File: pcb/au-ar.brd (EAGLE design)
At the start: 65 x 45 mm, 74 parts, among them U1 TPD12S520DBTR, U2 TPD12S521DBTR

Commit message: added final edits for v1 order and pcbway gerbers
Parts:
- added FLASH: 0532610571, volks73-Molex:PICOBLADE53261-0571
- moved R30 2.30 mm to (7.49, 23.9)
- moved R29 2.27 mm to (7.42, 21.6)
- moved C8 1.21 mm to (16.7, 6.55), turned to 270 degrees
- moved CAMERA1 0.60 mm to (58.2, 29.7)
- moved CAMERA2 0.37 mm to (58.2, 15.2)
- moved C3 0.25 mm to (23.9, 24.5)
- moved C7 0.08 mm to (27.3, 6.93)
- moved C10 0.05 mm to (3.86, 23.9), turned to 180 degrees
- renumbered LINE_2_1 to 1, LINE_2_2 to 2, LINE_2_3 to 3, LINE_2_4 to 4
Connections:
- net 5V: no longer B1.BB_1, B1.BB_50, B1.DB_1, B1.DB_50
- net GND: now also FLASH.1
- net SPI_CLK: now also FLASH.2
- net SPI_CS: now also FLASH.5
- net SPI_DI: now also FLASH.3
- net SPI_DO: now also FLASH.4
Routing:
- net 3V3: track 25.1 -> 97.9 mm, vias 11 -> 33
- net GND: track 108.4 -> 176.6 mm, vias 42 -> 78
- net 5V: track 2.63 -> 57.9 mm, vias 0 -> 10
- net SPI_CS: track 0.00 -> 34.3 mm, vias 0 -> 1
- net SPI_DO: track 0.00 -> 31.0 mm, vias 0 -> 1
- net SPI_CLK: track 0.00 -> 27.2 mm, vias 0 -> 1
- net SPI_DI: track 0.00 -> 24.1 mm, vias 0 -> 1
- net CEC1_FPGA: track 7.98 -> 24.8 mm, vias 0 -> 2
- net SCL1_FPGA: track 4.83 -> 18.2 mm, vias 0 -> 1
- net SDA1_FPGA: track 6.95 -> 19.9 mm, vias 0 -> 1
- net HP1_FPGA: track 2.49 -> 15.3 mm, vias 0 -> 1
- net N$13: track 0.00 -> 10.0 mm
- net N$14: track 0.00 -> 9.63 mm
- net N$15: track 0.00 -> 5.25 mm
- net N$16: track 0.00 -> 2.92 mm
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- added copper zone on layer 15, net 3V3
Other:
- board text added: "3.3V Pull Up"
- board text added: "Alchitry AU+AR Shield"
- board text added: "Dr. Daniel L. Lau Matt Ruffner Ying Yu University of Kentucky 2019"
- board text added: "GND CLK MOSI MISO CS"
- board text added: "LINE_1_1"
- board text added: "LINE_1_2"
- board text added: "LINE_1_3"
- board text added: "LINE_1_4"
- board text added: "LINE_2_1"
- board text added: "LINE_2_2"
- board text added: "LINE_2_3"
- board text added: "LINE_2_4"
- board text added: "Pull Down"
- board text added: "Series 0 Ohm Until Cut"

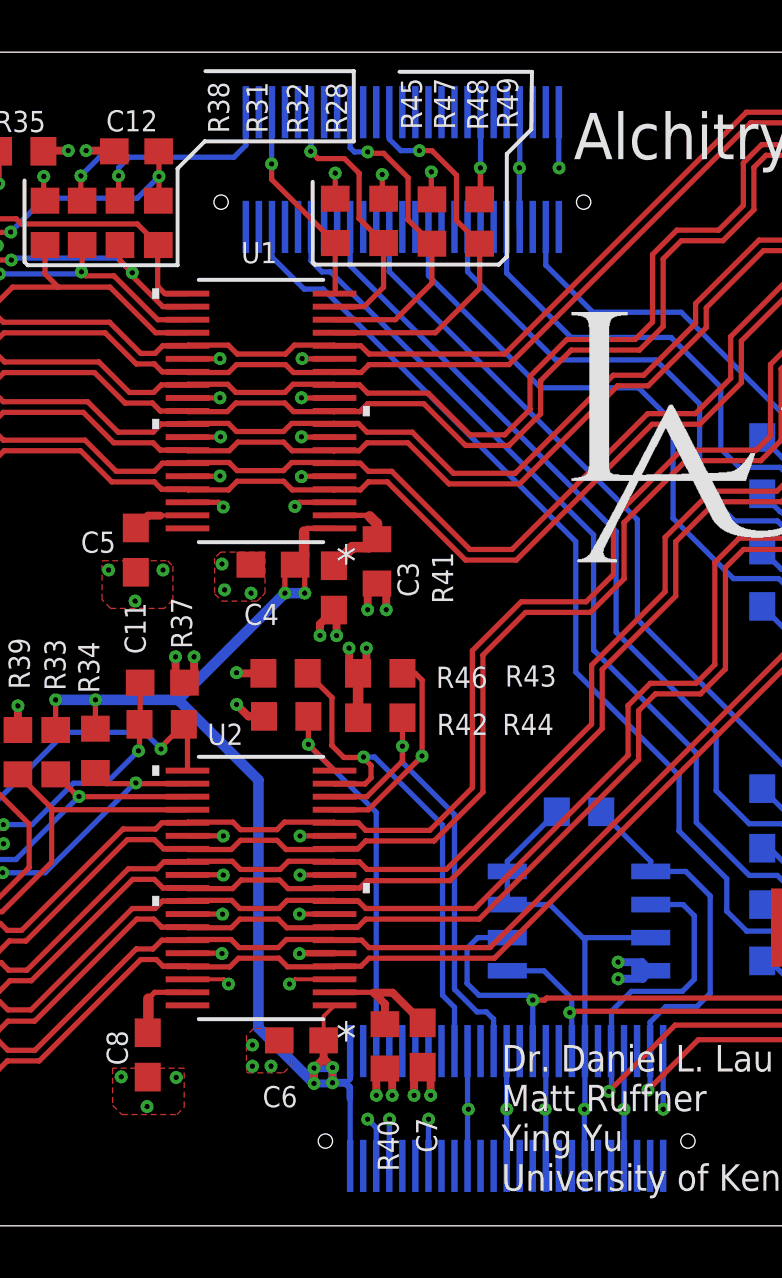
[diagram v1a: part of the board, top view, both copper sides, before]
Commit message: added external oscillator
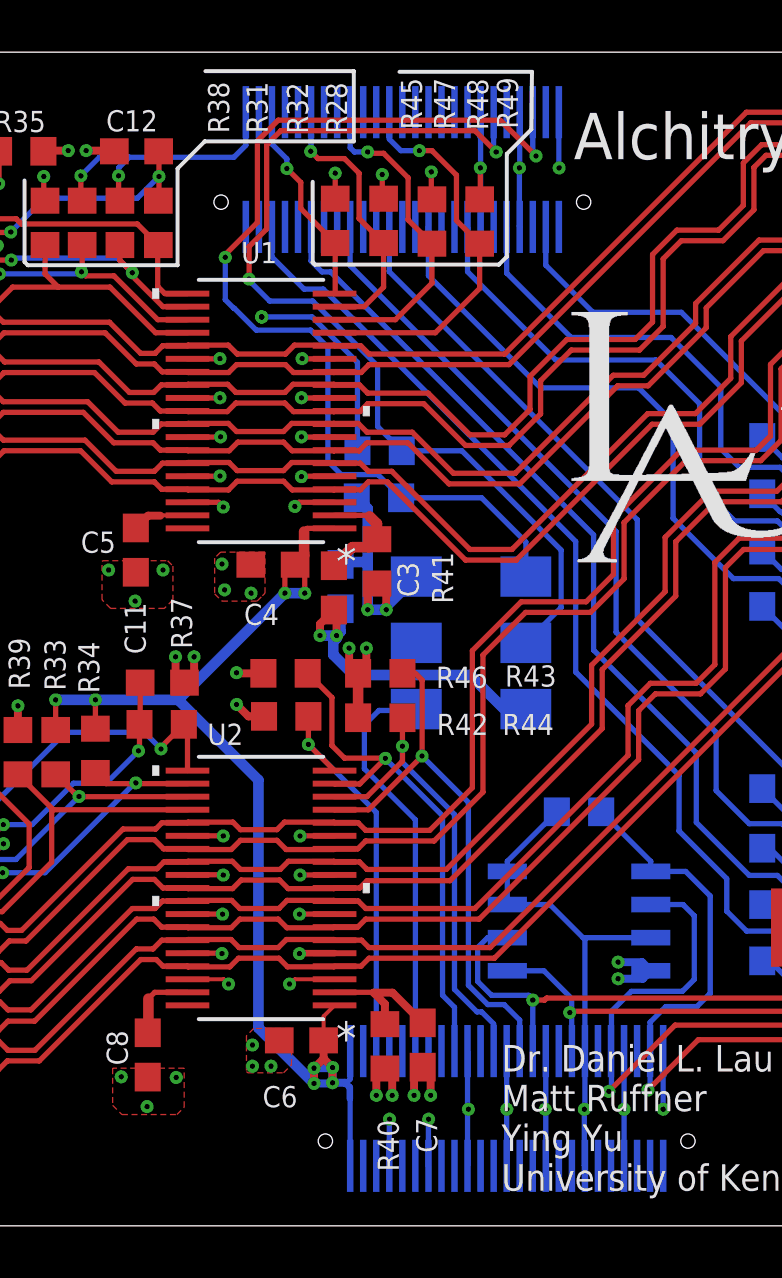
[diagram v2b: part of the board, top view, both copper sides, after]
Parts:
- added C1: 0.1uF, rcl:C0603
- added R27, R6: 3k, rcl:R0603
- added SI514: SI514, lupa300-components:XTAL-6PIN
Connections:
- new net OSC_CLK: B1.CB_45, SI514.P$4
- new net OSC_SCL: B1.AB_31, R27.1, SI514.P$2
- new net OSC_SDA: B1.AB_28, R6.1, SI514.P$1
- net 3V3: now also C1.1, R27.2, R6.2, SI514.P$6
- net CEC1_FPGA: now also B1.CB_37; no longer B1.CB_3
- net GND: now also C1.2, SI514.P$3
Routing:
- net OSC_SDA: track 0.00 -> 39.2 mm, vias 0 -> 2
- net OSC_SCL: track 0.00 -> 38.2 mm, vias 0 -> 2
- net 3V3: track 97.9 -> 113.8 mm, vias 33 -> 35
- net OSC_CLK: track 0.00 -> 15.6 mm
- net GND: track 176.6 -> 187.5 mm
- net CEC1_FPGA: track 24.8 -> 21.2 mm, vias 2 -> 1
- net SPI_CLK: track 27.2 -> 26.4 mm

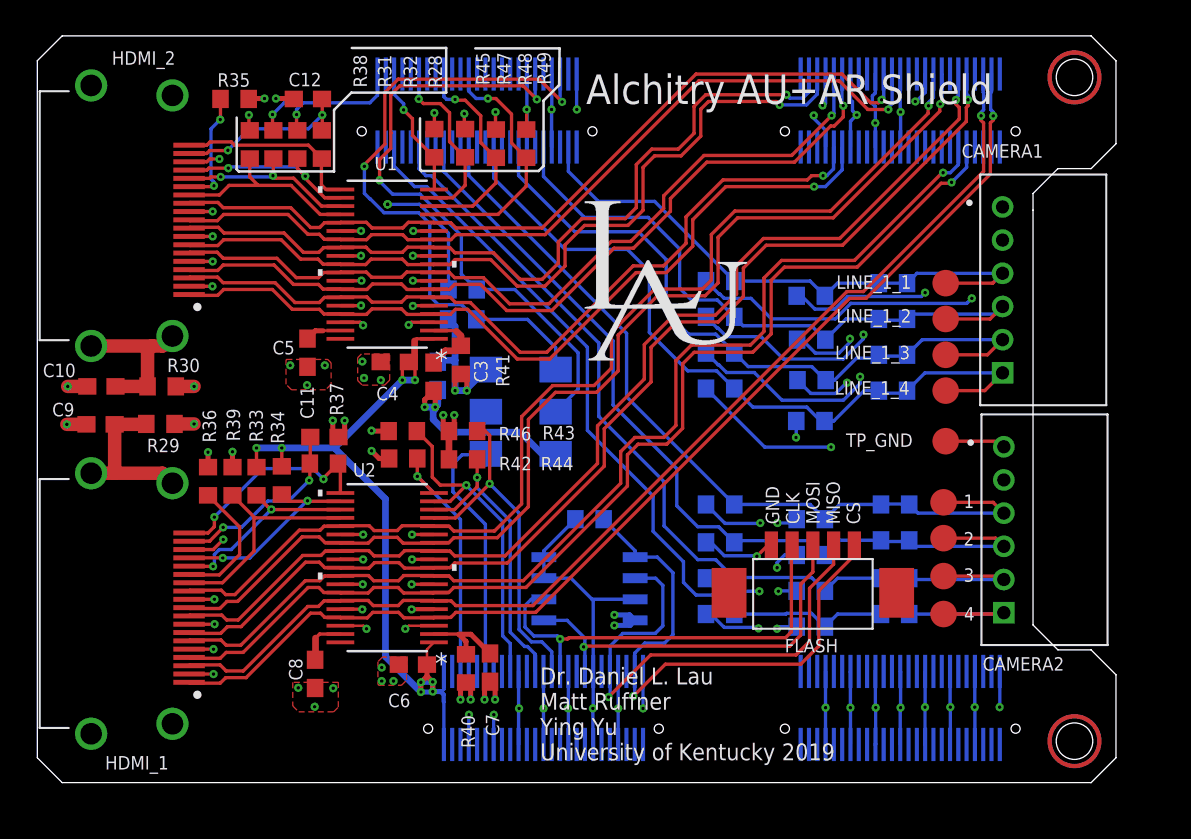
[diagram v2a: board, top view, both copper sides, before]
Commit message: started rerouting with new esd protection chips
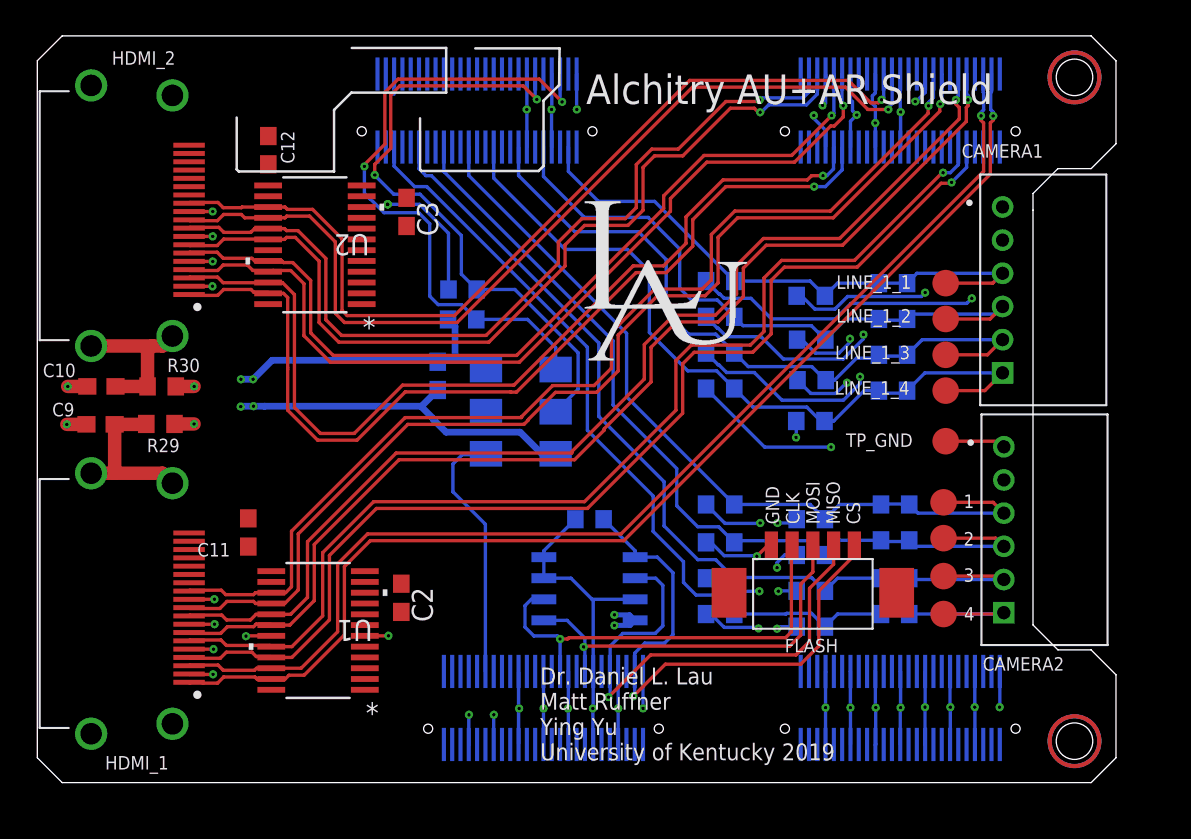
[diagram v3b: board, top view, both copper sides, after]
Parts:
- removed C4, C5, C6, C7, C8: 0.1uF, rcl:C0603
- removed R28, R37: 1k, rcl:R0603
- removed R31, R32, R33, R34, R43, R44, R46, R47, R48, R49: 47k, rcl:R0603
- removed R35: NP, rcl:R0603
- removed R36, R40, R41: 10k, rcl:R0603
- removed R38, R39: 27k, rcl:R0603
- removed R42, R45: 100k, rcl:R0603
- added C2: 0.1uF, rcl:C0603
- U1: value TPD12S520DBTR -> TPD12S016PWR; device TDP12S520:DBT38 -> lupa300-components:PW24
- U2: value TPD12S521DBTR -> TPD12S016PWR; device TDP12S521:DBT38 -> lupa300-components:PW24
- moved U1 22.5 mm to (16.9, 9.17)
- moved U2 19.9 mm to (16.7, 32.4)
- moved C3 10.1 mm to (22.3, 34.4)
- moved C11 7.36 mm to (12.7, 15.1), turned to 90 degrees
- moved C12 3.90 mm to (13.9, 38.1), turned to 90 degrees
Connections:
- removed net CEC1: HDMI_1.13, R39.2, U2.23
- removed net CEC1_FPGA: B1.CB_37, R43.1, U2.16
- removed net CEC2: HDMI_2.13, R38.2, U1.23
- removed net CEC2_FPGA: B1.AB_39, R49.1, U1.16
- removed net N$1: C5.1, U1.37
- removed net N$11: HDMI_1.14, R36.2
- removed net N$12: C3.1, R41.1, U1.2
- removed net N$15: C7.1, R40.1, U2.2
- removed net N$16: C8.1, U2.37
- removed net N$2: HDMI_2.14, R35.2
- new net CTHPD1: U1.12
- new net CTHPD2: U2.12
- new net LSOE1: B1.CB_37, U1.5
- new net LSOE2: B1.AB_39, U2.5
- net 3V3: now also U1.24, U2.24; no longer R38.1, R39.1, R40.2, R41.2, R42.2, R43.2, R44.2, R45.2, R46.2, R47.2, R48.2, R49.2
- net 5V: now also C2.1, C3.1, U1.11, U2.11; no longer C4.1, C6.1, R31.1, R32.1, R33.1, R34.1, U1.1, U2.1
- net 5VHDMI1: now also U1.13; no longer R37.1
- net 5VHDMI2: now also U2.13; no longer R28.1
- net CLK1_N: now also U1.15; no longer U2.15, U2.24
- net CLK1_P: now also U1.16; no longer U2.13, U2.26
- net CLK2_N: now also U2.15; no longer U1.15, U1.24
- net CLK2_P: now also U2.16; no longer U1.13, U1.26
- net D01_N: now also U1.17; no longer U2.12, U2.27
- net D01_P: now also U1.18; no longer U2.10, U2.29
- net D02_N: now also U2.17; no longer U1.12, U1.27
- net D02_P: now also U2.18; no longer U1.10, U1.29
- net D11_N: now also U1.20; no longer U2.30, U2.9
- net D11_P: now also U1.21; no longer U2.32, U2.7
- net D12_N: now also U2.20; no longer U1.30, U1.9
- net D12_P: now also U2.21; no longer U1.32, U1.7
- net D21_N: now also U1.22; no longer U2.33, U2.6
- net D21_P: now also U1.23; no longer U2.35, U2.4
- net D22_N: now also U2.22; no longer U1.33, U1.6
- net D22_P: now also U2.23; no longer U1.35, U1.4
- net GND: now also C2.2, U1.19, U1.6, U2.19, U2.6; no longer C4.2, C5.2, C6.2, C7.2, C8.2, R35.1, R36.1, U1.11, U1.25, U1.28, U1.3, U1.31, U1.34, U1.36, U1.5, U1.8, U2.11, U2.25, U2.28, U2.3, U2.31, U2.34, U2.36, U2.5, U2.8
- net HP1: now also U1.10; no longer R37.2, U2.20
- net HP1_FPGA: now also U1.4; no longer R42.1, U2.19
- net HP2: now also U2.10; no longer R28.2, U1.20
- net HP2_FPGA: now also U2.4; no longer R45.1, U1.19
- net SCL1: now also U1.8; no longer R33.2, U2.22
- net SCL1_FPGA: now also U1.2; no longer R44.1, U2.17
- net SCL2: now also U2.8; no longer R31.2, U1.22
- net SCL2_FPGA: now also U2.2; no longer R48.1, U1.17
- net SDA1: now also U1.9; no longer R34.2, U2.21
- net SDA1_FPGA: now also U1.3; no longer R46.1, U2.18
- net SDA2: now also U2.9; no longer R32.2, U1.21
- net SDA2_FPGA: now also U2.3; no longer R47.1, U1.18
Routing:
- net 5V: track 57.9 -> 0.00 mm, vias 10 -> 0
- net CEC1_FPGA: track 21.2 -> 0.00 mm, vias 1 -> 0
- net SDA1_FPGA: track 20.1 -> 0.00 mm, vias 1 -> 0
- net SCL1_FPGA: track 18.1 -> 0.00 mm, vias 1 -> 0
- net GND: track 187.5 -> 169.9 mm, vias 78 -> 39
- net HP1_FPGA: track 15.3 -> 0.00 mm, vias 1 -> 0
- net CEC2_FPGA: track 15.2 -> 0.00 mm, vias 1 -> 0
- net CEC1: track 13.8 -> 0.00 mm
- net HP1: track 13.4 -> 0.00 mm, vias 2 -> 0
- net SCL2_FPGA: track 12.8 -> 0.00 mm, vias 1 -> 0
- net SDA1: track 12.3 -> 0.00 mm, vias 2 -> 0
- net SCL1: track 12.2 -> 0.00 mm, vias 2 -> 0
- net CEC2: track 11.9 -> 0.00 mm
- net 5VHDMI1: track 11.4 -> 0.00 mm, vias 2 -> 0
- net HP2: track 11.4 -> 0.00 mm
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- removed copper zone on layer 1, net GND

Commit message: almost done routing
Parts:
- added C4, C5: 0.1uF, rcl:C0603
- moved C2 1.41 mm to (23.3, 11.1)
- moved C3 0.68 mm to (22.9, 34.7)
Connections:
- net 3V3: now also C4.1, C5.1
- net GND: now also C4.2, C5.2
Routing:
- net SDA2: track 0.00 -> 21.2 mm, vias 0 -> 2
- net SCL2: track 0.00 -> 21.0 mm, vias 0 -> 2
- net GND: track 169.9 -> 188.8 mm, vias 39 -> 55
- net SCL2_FPGA: track 0.00 -> 16.5 mm, vias 0 -> 2
- net HP2: track 0.00 -> 15.5 mm
- net SDA2_FPGA: track 0.00 -> 15.1 mm, vias 0 -> 2
- net 5V: track 0.00 -> 14.1 mm, vias 0 -> 1
- net HP2_FPGA: track 1.22 -> 14.1 mm, vias 0 -> 2
- net D11_N: track 65.5 -> 74.6 mm
- net D11_P: track 66.5 -> 75.5 mm
- net D02_P: track 52.7 -> 60.4 mm
- net D02_N: track 51.8 -> 59.5 mm
- net 5VHDMI2: track 0.00 -> 6.94 mm
- net D12_N: track 52.2 -> 58.5 mm
- net D12_P: track 53.5 -> 59.7 mm
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
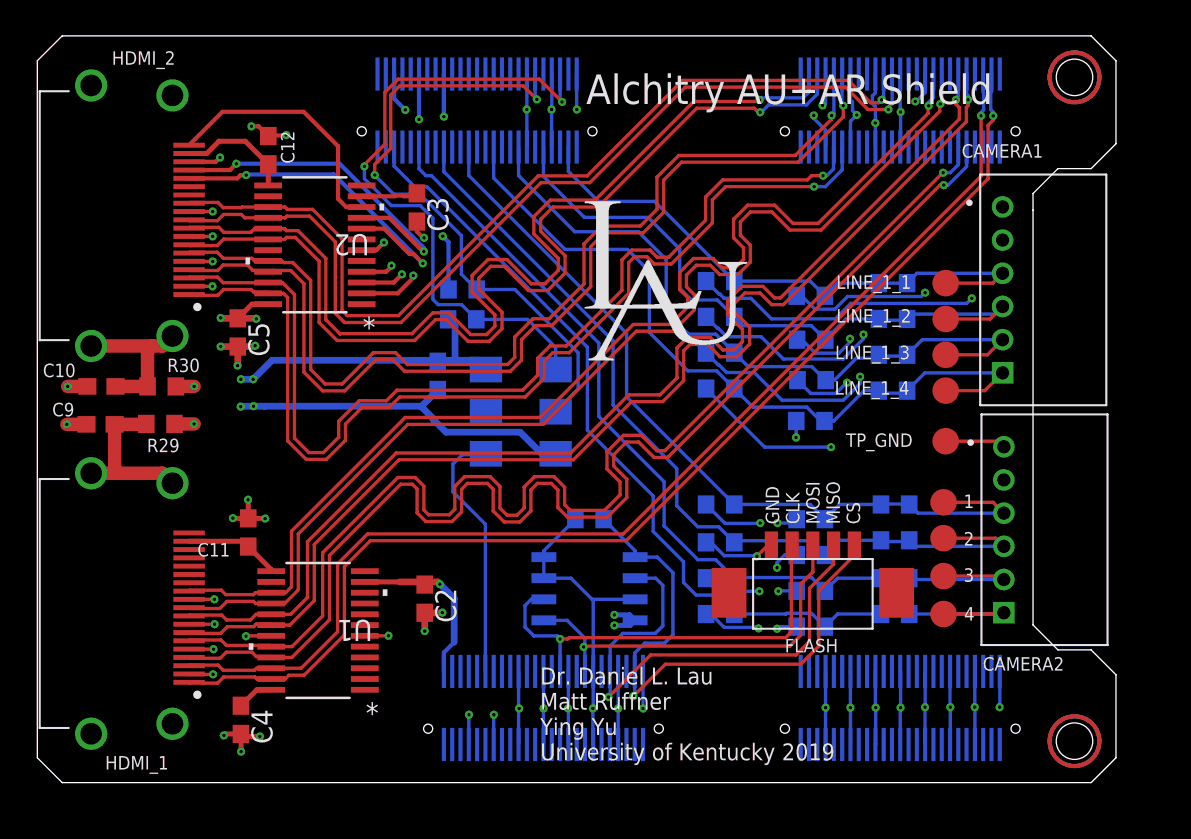
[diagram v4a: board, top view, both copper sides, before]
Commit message: need to add mosfet and order
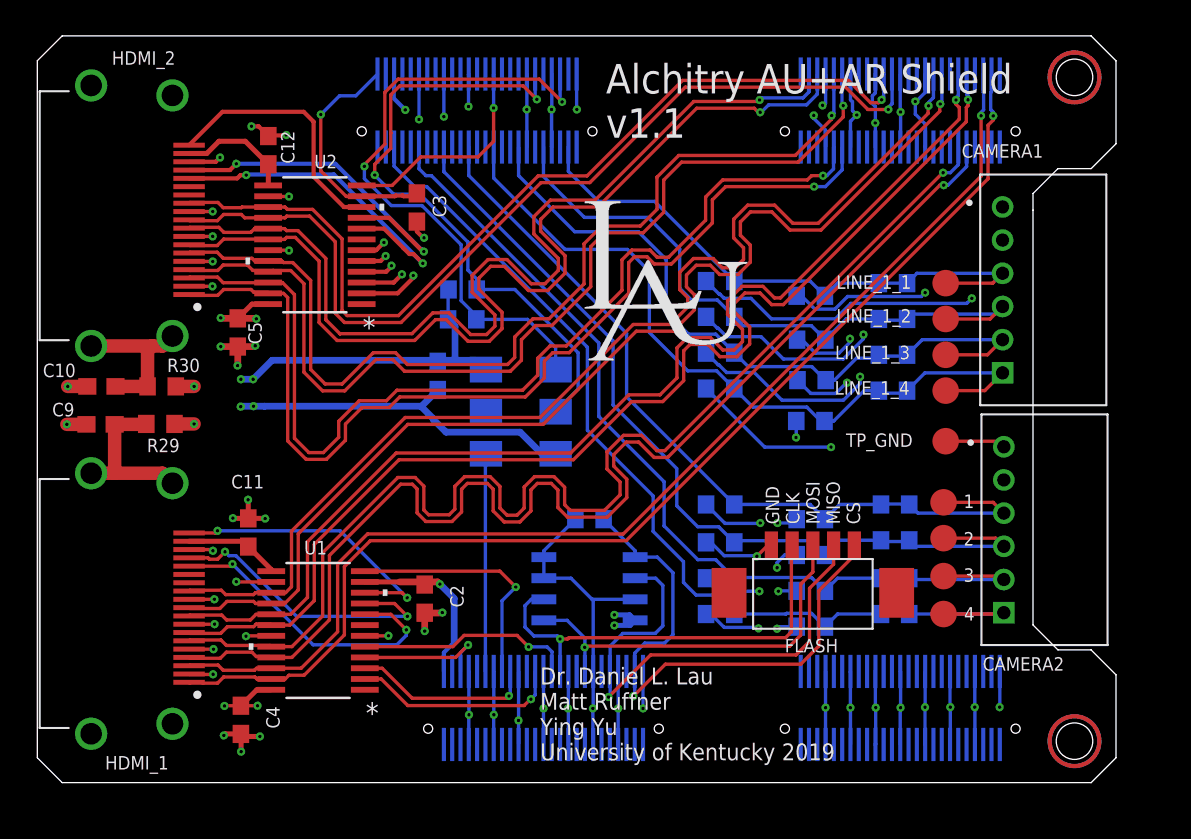
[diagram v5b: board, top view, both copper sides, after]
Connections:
- net 5V: no longer B1.AB_1
- net CTHPD1: now also B1.CB_43
- net CTHPD2: now also B1.AB_36
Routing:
- net LSOE2: track 0.00 -> 19.0 mm, vias 0 -> 2
- net SCL1: track 0.00 -> 18.6 mm, vias 0 -> 2
- net SDA1: track 0.00 -> 17.9 mm, vias 0 -> 2
- net HP1: track 0.00 -> 17.6 mm, vias 0 -> 2
- net CTHPD1: track 0.00 -> 14.9 mm, vias 0 -> 1
- net LSOE1: track 0.00 -> 13.2 mm, vias 0 -> 1
- net CTHPD2: track 0.00 -> 13.1 mm, vias 0 -> 1
- net SCL1_FPGA: track 0.00 -> 12.6 mm, vias 0 -> 1
- net GND: track 188.8 -> 200.5 mm, vias 55 -> 59
- net SDA1_FPGA: track 0.00 -> 11.0 mm, vias 0 -> 1
- net 5V: track 14.1 -> 25.0 mm, vias 1 -> 2
- net HP1_FPGA: track 0.00 -> 8.32 mm, vias 0 -> 1
- net 3V3: track 109.3 -> 112.4 mm, vias 25 -> 26
- net OSC_CLK: track 15.6 -> 13.1 mm
- net OSC_SDA: track 38.9 -> 38.2 mm
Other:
- board text added: "Alchitry AU+AR Shield v1.1"
- board text removed: "Alchitry AU+AR Shield"
